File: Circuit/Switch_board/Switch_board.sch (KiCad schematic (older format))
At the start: 17 parts

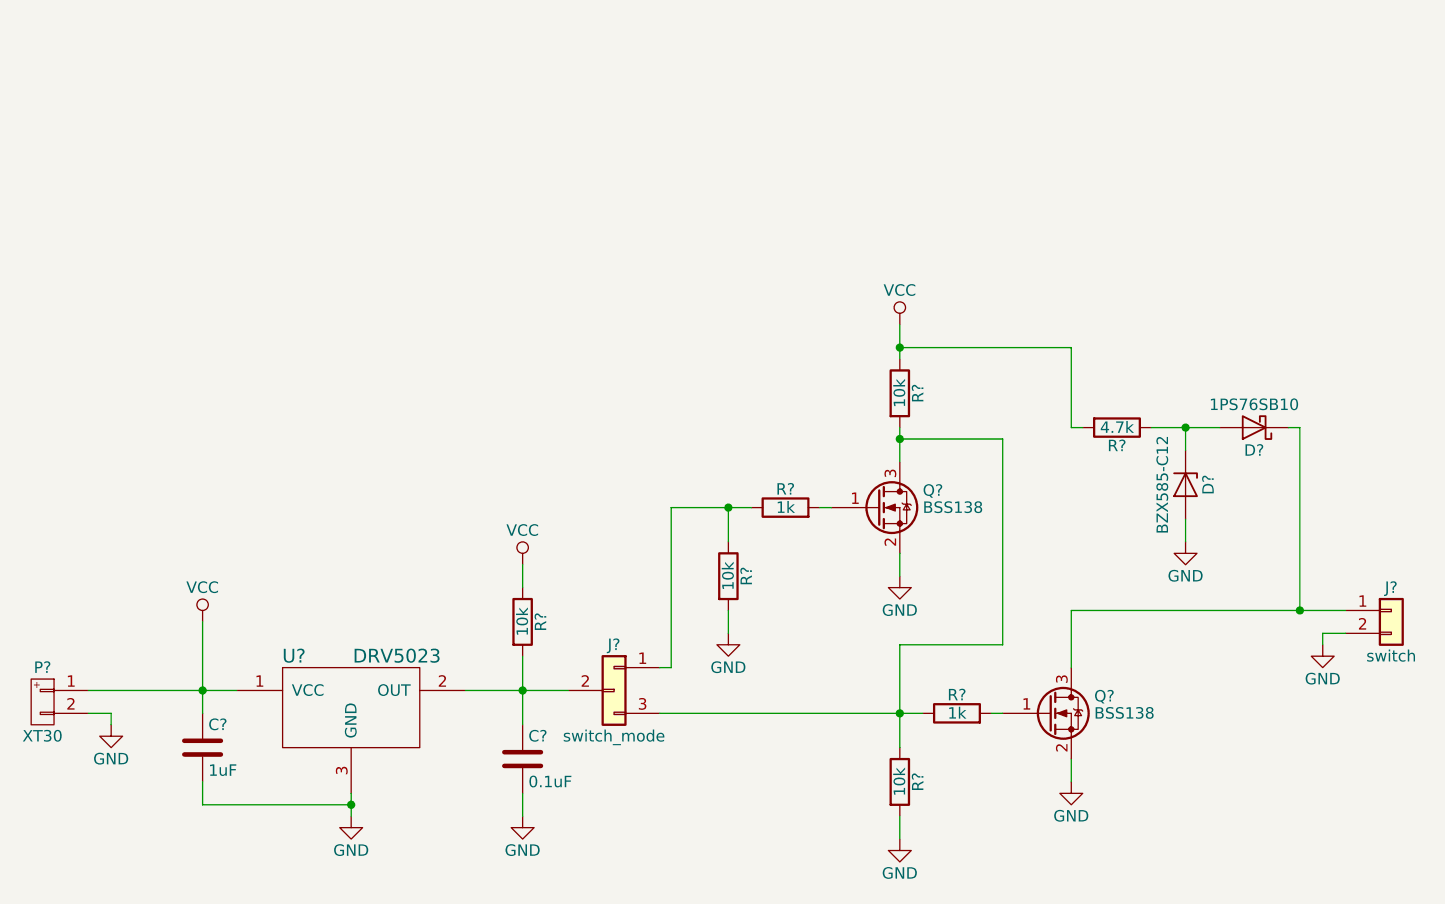
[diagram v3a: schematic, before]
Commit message: annotated schematic and added PWR_FLAG to switch_board
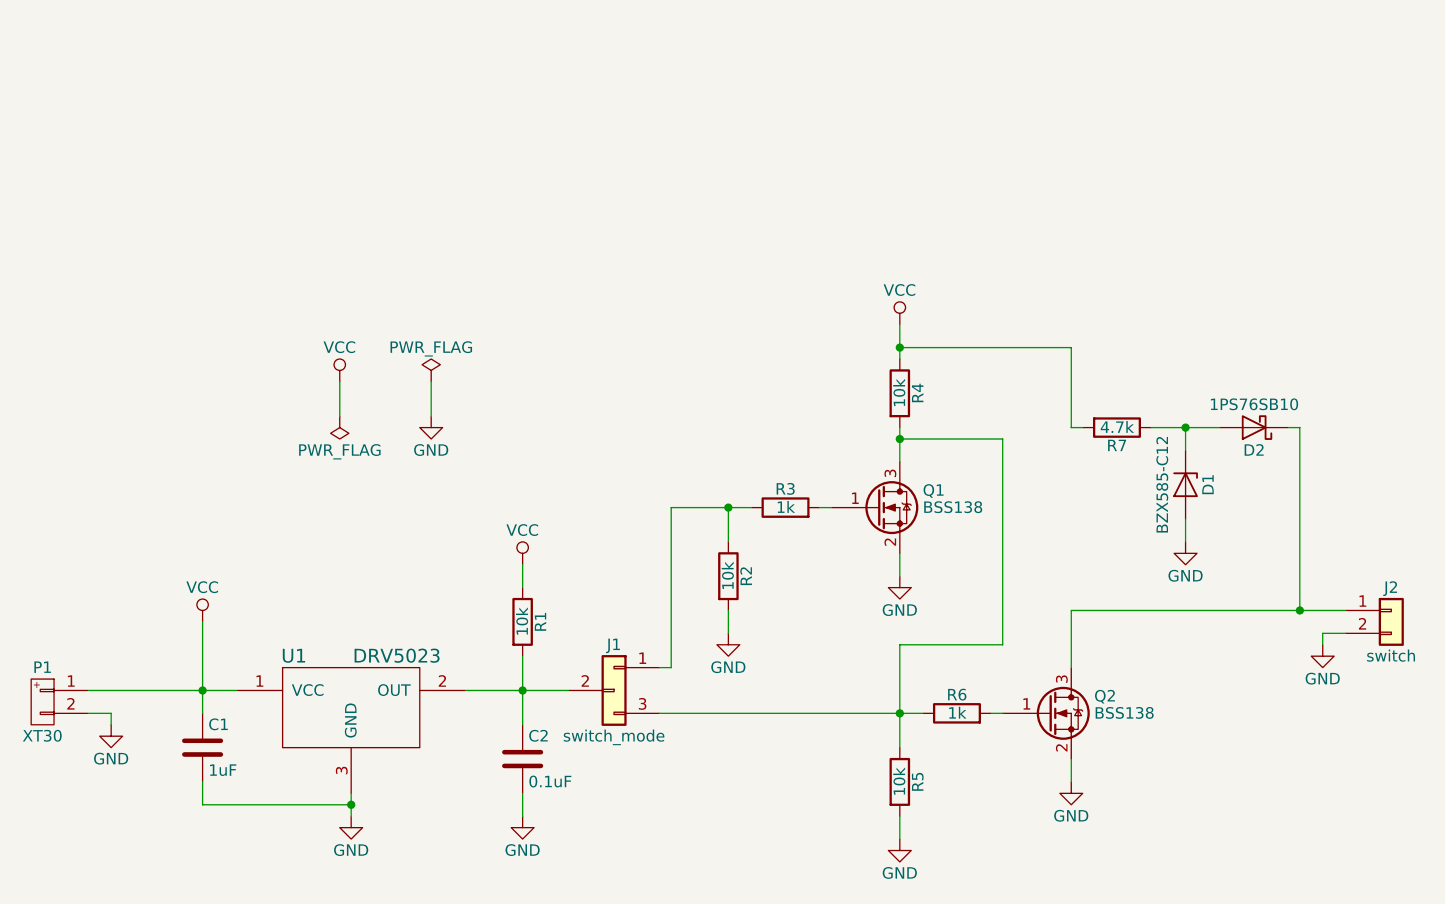
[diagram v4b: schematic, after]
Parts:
- gave numbers to parts that had none: 17
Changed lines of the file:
@@
 $EndDescr
 $Comp
-L XT30 P?
+L XT30 P1
 U 1 1 5A826541
 P 2350 4250
-F 0 "P?" H 2350 4400 50  0000 C CNN
+F 0 "P1" H 2350 4400 50  0000 C CNN
 F 1 "XT30" H 2350 4100 50  0000 C CNN
 F 2 "zeabus:XT30" H 2350 4250 60  0001 C CNN
@@
 $EndComp
 $Comp
-L DRV5023 U?
+L DRV5023 U1
 U 1 1 5A8265E8
 P 3700 4200
-F 0 "U?" H 3450 4350 60  0000 C CNN
+F 0 "U1" H 3450 4350 60  0000 C CNN
 F 1 "DRV5023" H 3900 4350 60  0000 C CNN
 F 2 "TO_SOT_Packages_SMD:SOT-23_Handsoldering" H 3700 4200 60  0001 C CNN
@@
 $EndComp
 $Comp
-L C C?
+L C C1
 U 1 1 5A8266C7
 P 3050 4450
-F 0 "C?" H 3075 4550 50  0000 L CNN
+F 0 "C1" H 3075 4550 50  0000 L CNN
 F 1 "1uF" H 3075 4350 50  0000 L CNN
 F 2 "Capacitors_SMD:C_0603_HandSoldering" H 3088 4300 50  0001 C CNN
@@
 $EndComp
 $Comp
-L GND #PWR?
+L GND #PWR01
 U 1 1 5A826833
 P 3700 4750
-F 0 "#PWR?" H 3700 4500 50  0001 C CNN
+F 0 "#PWR01" H 3700 4500 50  0001 C CNN
 F 1 "GND" H 3700 4600 50  0000 C CNN
 F 2 "" H 3700 4750 50  0001 C CNN
@@
 $EndComp
 $Comp
-L GND #PWR?
+L GND #PWR02
 U 1 1 5A826918
 P 2650 4350
-F 0 "#PWR?" H 2650 4100 50  0001 C CNN
+F 0 "#PWR02" H 2650 4100 50  0001 C CNN
 F 1 "GND" H 2650 4200 50  0000 C CNN
 F 2 "" H 2650 4350 50  0001 C CNN
@@
 $EndComp
 $Comp
-L R R?
+L R R1
 U 1 1 5A826B45
 P 4450 3900
-F 0 "R?" V 4530 3900 50  0000 C CNN
+F 0 "R1" V 4530 3900 50  0000 C CNN
 F 1 "10k" V 4450 3900 50  0000 C CNN
 F 2 "Resistors_SMD:R_0603_HandSoldering" V 4380 3900 50  0001 C CNN
@@
 $EndComp
 $Comp
-L Conn_01x03_Selection_Source J?
+L Conn_01x03_Selection_Source J1
 U 1 1 5A82740B
 P 4850 4200
-F 0 "J?" H 4850 4400 50  0000 C CNN
+F 0 "J1" H 4850 4400 50  0000 C CNN
 F 1 "switch_mode" H 4850 4000 50  0000 C CNN
 F 2 "Pin_Headers:Pin_Header_Straight_1x03_Pitch2.54mm" H 4900 4200 50  0001 C CNN
@@
 $EndComp
 $Comp
-L Conn_01x02 J?
+L Conn_01x02 J2
 U 1 1 5A82779E
 P 8250 3850
-F 0 "J?" H 8250 3950 50  0000 C CNN
+F 0 "J2" H 8250 3950 50  0000 C CNN
 F 1 "switch" H 8250 3650 50  0000 C CNN
 F 2 "zeabus:90136-1202" H 8250 3850 50  0001 C CNN
@@
 $EndComp
 $Comp
-L R R?
+L R R2
 U 1 1 5A82867B
 P 5350 3700
-F 0 "R?" V 5430 3700 50  0000 C CNN
+F 0 "R2" V 5430 3700 50  0000 C CNN
 F 1 "10k" V 5350 3700 50  0000 C CNN
 F 2 "Resistors_SMD:R_0603_HandSoldering" V 5280 3700 50  0001 C CNN
@@
 $EndComp
 $Comp
-L R R?
+L R R3
 U 1 1 5A8289F3
 P 5600 3400
-F 0 "R?" V 5680 3400 50  0000 C CNN
+F 0 "R3" V 5680 3400 50  0000 C CNN
 F 1 "1k" V 5600 3400 50  0000 C CNN
 F 2 "Resistors_SMD:R_0603_HandSoldering" V 5530 3400 50  0001 C CNN
@@
 $EndComp
 $Comp
-L GND #PWR?
+L GND #PWR03
 U 1 1 5A829801
 P 7950 4000
-F 0 "#PWR?" H 7950 3750 50  0001 C CNN
+F 0 "#PWR03" H 7950 3750 50  0001 C CNN
 F 1 "GND" H 7950 3850 50  0000 C CNN
 F 2 "" H 7950 4000 50  0001 C CNN
@@
 $EndComp
 $Comp
-L GND #PWR?
+L GND #PWR04
 U 1 1 5A829CAE
 P 5350 3950
-F 0 "#PWR?" H 5350 3700 50  0001 C CNN
+F 0 "#PWR04" H 5350 3700 50  0001 C CNN
 F 1 "GND" H 5350 3800 50  0000 C CNN
 F 2 "" H 5350 3950 50  0001 C CNN
@@
 $EndComp
 $Comp
-L BSS138 Q?
+L BSS138 Q1
 U 1 1 5A856C21
 P 6000 3400
-F 0 "Q?" H 6200 3475 50  0000 L CNN
+F 0 "Q1" H 6200 3475 50  0000 L CNN
 F 1 "BSS138" H 6200 3400 50  0000 L CNN
 F 2 "TO_SOT_Packages_SMD:SOT-23_Handsoldering" H 6200 3325 50  0001 L CIN
@@
 $EndComp
 $Comp
-L C C?
+L C C2
 U 1 1 5A883823
 P 4450 4500
-F 0 "C?" H 4475 4600 50  0000 L CNN
+F 0 "C2" H 4475 4600 50  0000 L CNN
 F 1 "0.1uF" H 4475 4400 50  0000 L CNN
 F 2 "Capacitors_SMD:C_0603_HandSoldering" H 4488 4350 50  0001 C CNN
@@
 $EndComp
 $Comp
-L GND #PWR?
+L GND #PWR05
 U 1 1 5A883892
 P 4450 4750
-F 0 "#PWR?" H 4450 4500 50  0001 C CNN
+F 0 "#PWR05" H 4450 4500 50  0001 C CNN
 F 1 "GND" H 4450 4600 50  0000 C CNN
 F 2 "" H 4450 4750 50  0001 C CNN
@@
 $EndComp
 $Comp
-L GND #PWR?
+L GND #PWR06
 U 1 1 5A88921C
 P 6100 3700
-F 0 "#PWR?" H 6100 3450 50  0001 C CNN
+F 0 "#PWR06" H 6100 3450 50  0001 C CNN
 F 1 "GND" H 6100 3550 50  0000 C CNN
 F 2 "" H 6100 3700 50  0001 C CNN
@@
 $EndComp
 $Comp
-L R R?
+L R R7
 U 1 1 5A88CB30
 P 7050 3050
-F 0 "R?" V 7130 3050 50  0000 C CNN
+F 0 "R7" V 7130 3050 50  0000 C CNN
 F 1 "4.7k" V 7050 3050 50  0000 C CNN
 F 2 "Resistors_SMD:R_0603_HandSoldering" V 6980 3050 50  0001 C CNN
@@
 	4450 4750 4450 4650
 $Comp
-L D_Zener D?
+L D_Zener D1
 U 1 1 5A89D38A
 P 7350 3300
-F 0 "D?" H 7350 3400 50  0000 C CNN
+F 0 "D1" H 7350 3400 50  0000 C CNN
 F 1 "BZX585-C12" H 7350 3200 50  0000 C CNN
 F 2 "Diodes_SMD:D_SOD-523" H 7350 3300 50  0001 C CNN
@@
 $EndComp
 $Comp
-L VCC #PWR?
+L VCC #PWR07
 U 1 1 5A89DB47
 P 3050 3900
-F 0 "#PWR?" H 3050 3750 50  0001 C CNN
+F 0 "#PWR07" H 3050 3750 50  0001 C CNN
 F 1 "VCC" H 3050 4050 50  0000 C CNN
 F 2 "" H 3050 3900 50  0001 C CNN
@@
 $EndComp
 $Comp
-L VCC #PWR?
-U 1 1 5A89E7B6
-P 4450 3650
-F 0 "#PWR?" H 4450 3500 50  0001 C CNN
-F 1 "VCC" H 4450 3800 50  0000 C CNN
-F 2 "" H 4450 3650 50  0001 C CNN
-F 3 "" H 4450 3650 50  0001 C CNN
-	1    4450 3650
-	1    0    0    -1
-$EndComp
-$Comp
-L D_Schottky D?
+L D_Schottky D2
 U 1 1 5A89F23A
 P 7650 3050
-F 0 "D?" H 7650 3150 50  0000 C CNN
+F 0 "D2" H 7650 3150 50  0000 C CNN
 F 1 "1PS76SB10" H 7650 2950 50  0000 C CNN
 F 2 "Diodes_SMD:D_SOD-323_HandSoldering" H 7650 3050 50  0001 C CNN
@@
 $EndComp
 $Comp
-L GND #PWR?
+L GND #PWR08
 U 1 1 5A89F539
 P 7350 3550
-F 0 "#PWR?" H 7350 3300 50  0001 C CNN
+F 0 "#PWR08" H 7350 3300 50  0001 C CNN
 F 1 "GND" H 7350 3400 50  0000 C CNN
 F 2 "" H 7350 3550 50  0001 C CNN
@@
 Connection ~ 5350 3400
 $Comp
-L R R?
+L R R5
 U 1 1 5A8DDCD9
 P 6100 4600
-F 0 "R?" V 6180 4600 50  0000 C CNN
+F 0 "R5" V 6180 4600 50  0000 C CNN
 F 1 "10k" V 6100 4600 50  0000 C CNN
 F 2 "Resistors_SMD:R_0603_HandSoldering" V 6030 4600 50  0001 C CNN
@@
 $EndComp
 $Comp
-L R R?
+L R R6
 U 1 1 5A8DDCDF
 P 6350 4300
-F 0 "R?" V 6430 4300 50  0000 C CNN
+F 0 "R6" V 6430 4300 50  0000 C CNN
 F 1 "1k" V 6350 4300 50  0000 C CNN
 F 2 "Resistors_SMD:R_0603_HandSoldering" V 6280 4300 50  0001 C CNN
@@
 $EndComp
 $Comp
-L GND #PWR?
+L GND #PWR09
 U 1 1 5A8DDCE5
 P 6100 4850
-F 0 "#PWR?" H 6100 4600 50  0001 C CNN
+F 0 "#PWR09" H 6100 4600 50  0001 C CNN
 F 1 "GND" H 6100 4700 50  0000 C CNN
 F 2 "" H 6100 4850 50  0001 C CNN
@@
 $EndComp
 $Comp
-L BSS138 Q?
+L BSS138 Q2
 U 1 1 5A8DDCEB
 P 6750 4300
-F 0 "Q?" H 6950 4375 50  0000 L CNN
+F 0 "Q2" H 6950 4375 50  0000 L CNN
 F 1 "BSS138" H 6950 4300 50  0000 L CNN
 F 2 "TO_SOT_Packages_SMD:SOT-23_Handsoldering" H 6950 4225 50  0001 L CIN
@@
 $EndComp
 $Comp
-L GND #PWR?
+L GND #PWR010
 U 1 1 5A8DDCF1
 P 6850 4600
-F 0 "#PWR?" H 6850 4350 50  0001 C CNN
+F 0 "#PWR010" H 6850 4350 50  0001 C CNN
 F 1 "GND" H 6850 4450 50  0000 C CNN
 F 2 "" H 6850 4600 50  0001 C CNN
@@
 	5100 4100 5100 3400
 $Comp
-L VCC #PWR?
+L VCC #PWR011
 U 1 1 5A8DFBDA
 P 6100 2600
-F 0 "#PWR?" H 6100 2450 50  0001 C CNN
+F 0 "#PWR011" H 6100 2450 50  0001 C CNN
 F 1 "VCC" H 6100 2750 50  0000 C CNN
 F 2 "" H 6100 2600 50  0001 C CNN
@@
 $EndComp
 $Comp
-L R R?
+L R R4
 U 1 1 5A8DFC36
 P 6100 2900
-F 0 "R?" V 6180 2900 50  0000 C CNN
+F 0 "R4" V 6180 2900 50  0000 C CNN
 F 1 "10k" V 6100 2900 50  0000 C CNN
 F 2 "Resistors_SMD:R_0603_HandSoldering" V 6030 2900 50  0001 C CNN
@@
 Wire Wire Line
 	4200 4200 4650 4200
+$Comp
+L VCC #PWR012
+U 1 1 5A89E7B6
+P 4450 3650
+F 0 "#PWR012" H 4450 3500 50  0001 C CNN
+F 1 "VCC" H 4450 3800 50  0000 C CNN
+F 2 "" H 4450 3650 50  0001 C CNN
+F 3 "" H 4450 3650 50  0001 C CNN
+	1    4450 3650
+	1    0    0    -1
+$EndComp
+$Comp
+L PWR_FLAG #FLG013
+U 1 1 5A8DF01C
+P 4050 2850
+F 0 "#FLG013" H 4050 2925 50  0001 C CNN
+F 1 "PWR_FLAG" H 4050 3000 50  0000 C CNN
+F 2 "" H 4050 2850 50  0001 C CNN
+F 3 "" H 4050 2850 50  0001 C CNN
+	1    4050 2850
+	1    0    0    -1
+$EndComp
+$Comp
+L PWR_FLAG #FLG014
+U 1 1 5A8DF1C6
+P 3650 3000
+F 0 "#FLG014" H 3650 3075 50  0001 C CNN
+F 1 "PWR_FLAG" H 3650 3150 50  0000 C CNN
+F 2 "" H 3650 3000 50  0001 C CNN
+F 3 "" H 3650 3000 50  0001 C CNN
+	1    3650 3000
+	-1   0    0    1
+$EndComp
+$Comp
+L VCC #PWR015
+U 1 1 5A8E00E8
+P 3650 2850
+F 0 "#PWR015" H 3650 2700 50  0001 C CNN
+F 1 "VCC" H 3650 3000 50  0000 C CNN
+F 2 "" H 3650 2850 50  0001 C CNN
+F 3 "" H 3650 2850 50  0001 C CNN
+	1    3650 2850
+	1    0    0    -1
+$EndComp
+$Comp
+L GND #PWR016
+U 1 1 5A8E04F5
+P 4050 3000
+F 0 "#PWR016" H 4050 2750 50  0001 C CNN
+F 1 "GND" H 4050 2850 50  0000 C CNN
+F 2 "" H 4050 3000 50  0001 C CNN
+F 3 "" H 4050 3000 50  0001 C CNN
+	1    4050 3000
+	1    0    0    -1
+$EndComp
+Wire Wire Line
+	3650 2850 3650 3000
+Wire Wire Line
+	4050 2850 4050 3000
 $EndSCHEMATC
